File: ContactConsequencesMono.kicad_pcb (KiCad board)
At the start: 2 copper layers, 135 x 124 mm, 183 parts, among them IC1 TPD2E1B06, IC2 TPS73633, IC3 MCP73831/2-OT, IC4 TPS73618, IC5 MCP1640-SOT, IC6 TPS73633, J1 ISP, J10 PWM, J11 Sense1, J12 Sense2, J13 IO1, J14 IO2, J15 I2C, J16 Serial, J17 I2S, J2 Line in, J3 Line out, J4 SD_Card, J5 shield, J6 USB_OTG, J7 Battery, J8 Display - secondary, J9 Display - main, Q1 Q_PMOS_GSD, SW1 Reset, SW2 Charge select, SW3 sw_vol, SW4 Rotary_Encoder, SW5 sw_fadein, SW6 sw_fadeout, SW7 sw_touch, SW8 sw_mode, SW9 sw_release, U1 ATMEGA32U4-AU, U2 vs1053b, U3 MAX9723-TQFN, U4 MAX7219, U5 TCA9534, U6 TXS0108EPWR, Y1 16MHz, Y2 12,288MHz

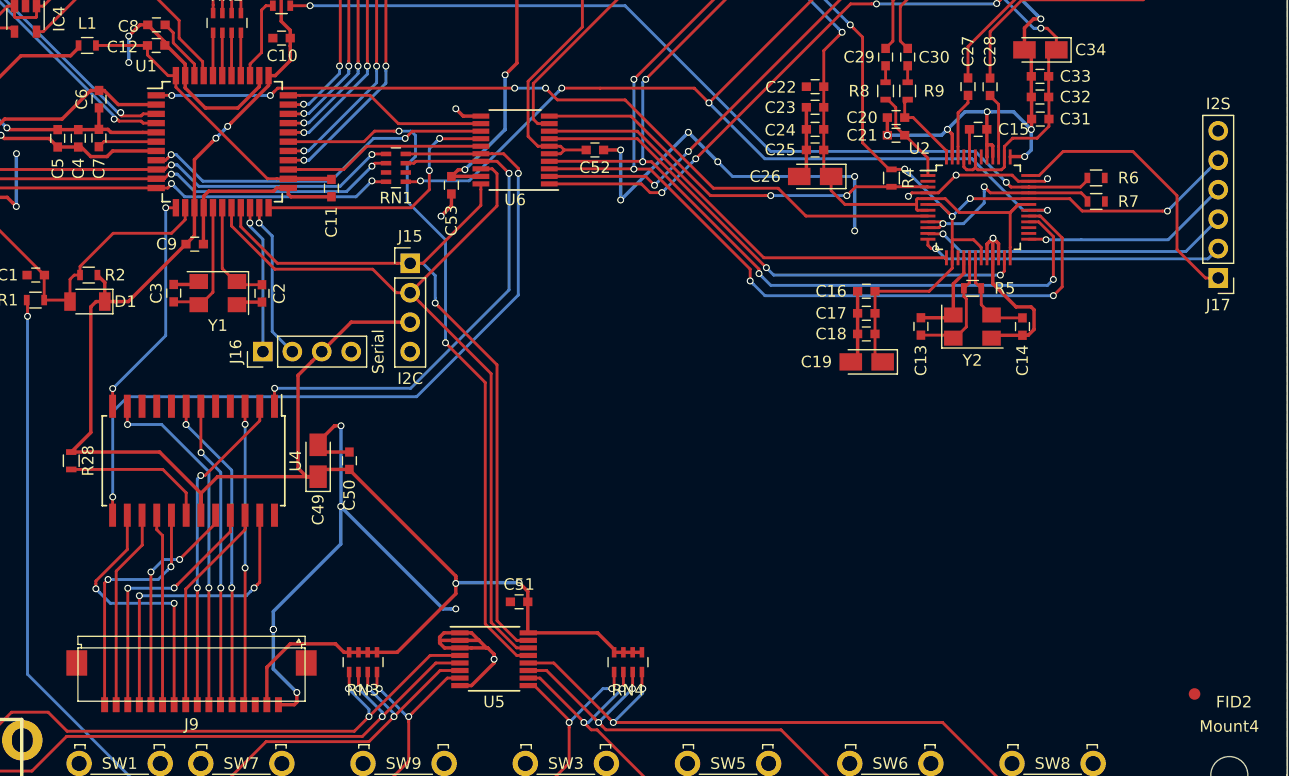
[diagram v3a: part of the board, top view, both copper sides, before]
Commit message: v0.1 ok for fab. Quote asked to PCB maker.
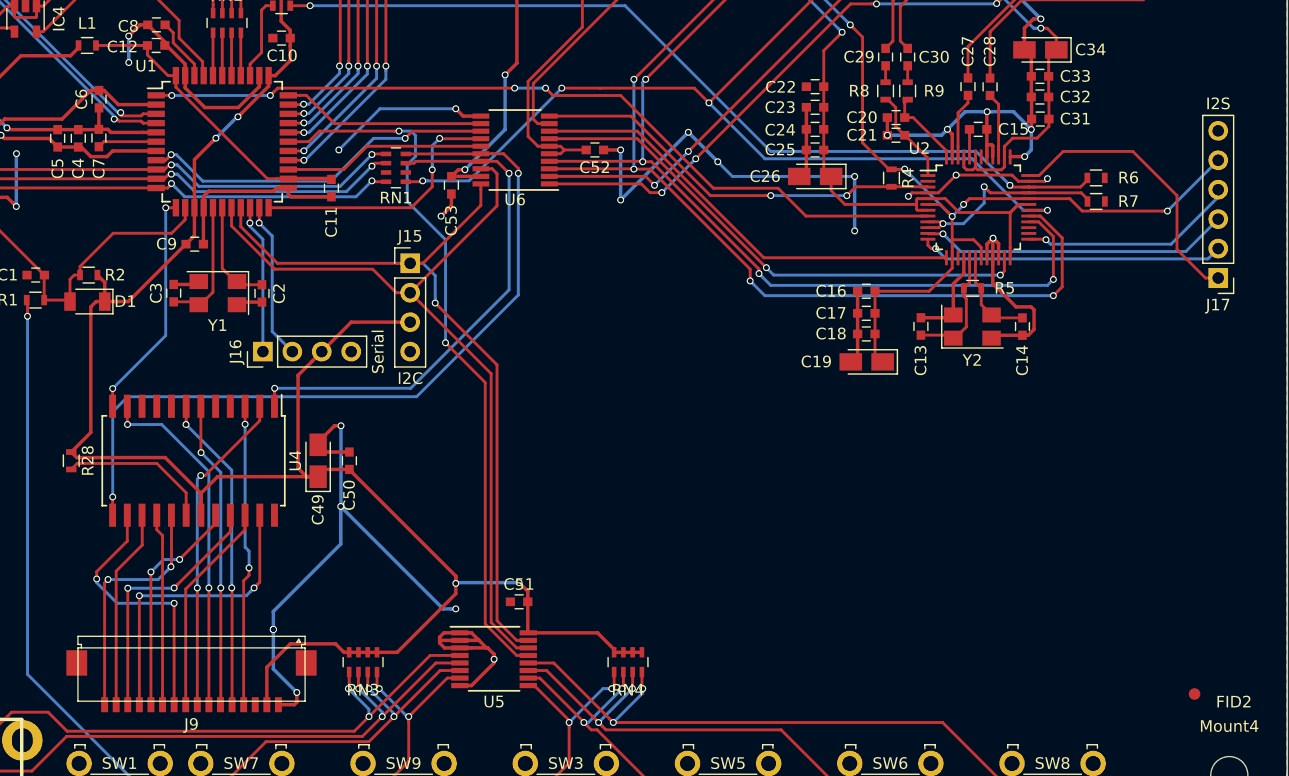
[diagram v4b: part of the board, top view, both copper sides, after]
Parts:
- added svg2mod: G***, Logos:cc_Silk_60mm, B.Cu at (171.1, 117.6)
- added svg2mod: G***, Logos:cc_noms, B.Cu at (145.2, 134.0)
- added svg2mod: G***, Logos:cc_capacitivemusicplayer, B.Cu at (148.8, 66.3)
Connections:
- SW4 pad 4: DGND -> (no net)
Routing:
- net DGND: track 342.5 -> 354.1 mm, vias 33 -> 34
- net I2S_MCK: track 18.2 -> 18.8 mm
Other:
- board text added: "XI/2017"
- board text added: "v0.1"

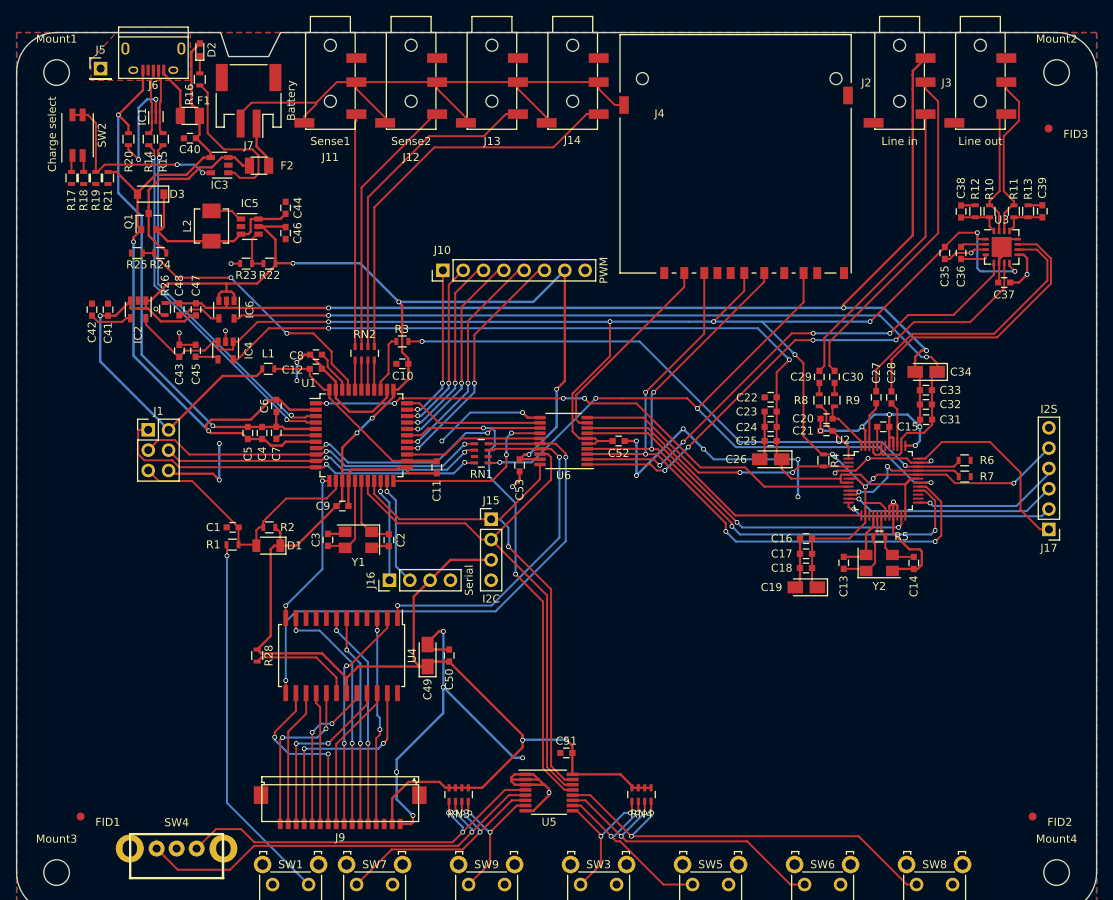
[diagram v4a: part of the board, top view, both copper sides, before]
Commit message: Updated project with connector for main power switch. Modified fabrication files.
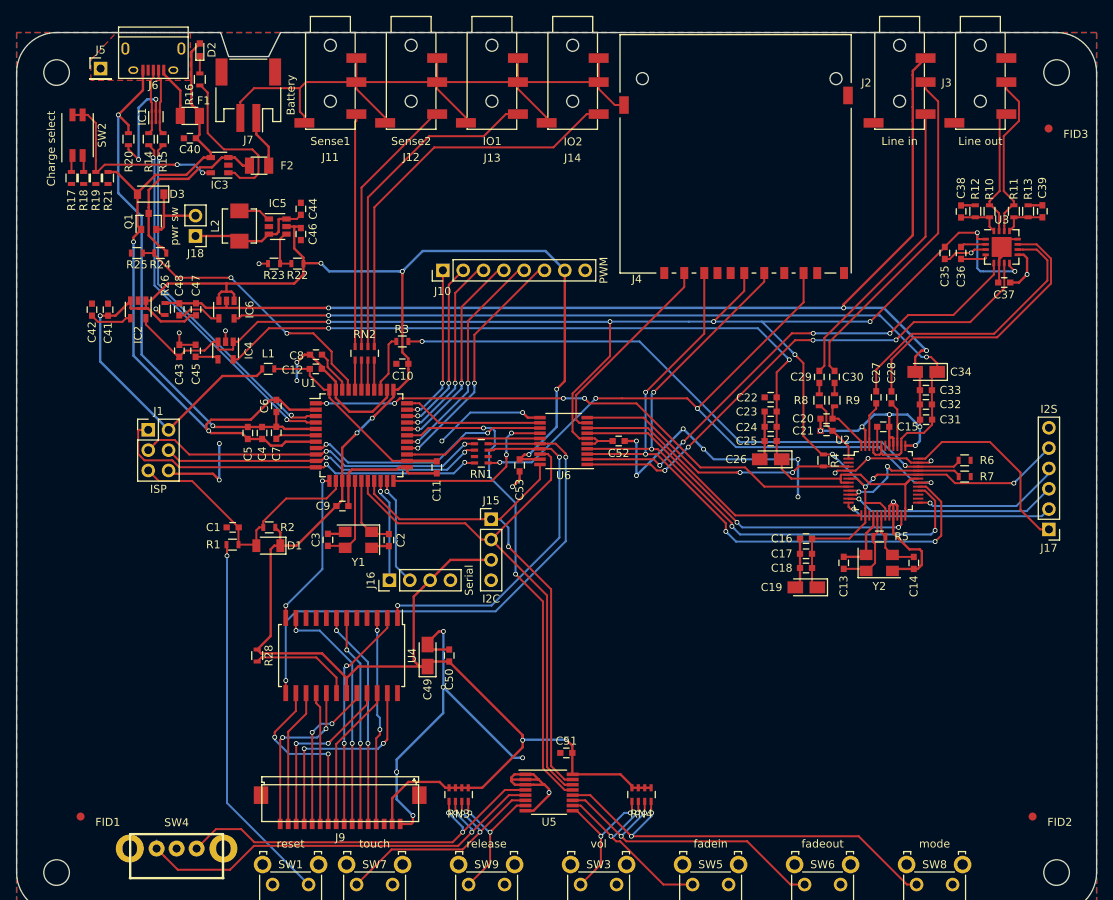
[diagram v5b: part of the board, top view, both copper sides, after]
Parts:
- added J18: pwr sw, Pin_Headers:Pin_Header_Straight_1x02_Pitch2.54mm, F.Cu at (102.4, 65.4)
- SW1: value Reset -> reset
- SW3: value sw_vol -> vol
- SW5: value sw_fadein -> fadein
- SW6: value sw_fadeout -> fadeout
- SW7: value sw_touch -> touch
- SW8: value sw_mode -> mode
- SW9: value sw_release -> release
- moved svg2mod 5.71 mm to (154.0, 63.9)
- moved R22 3.49 mm to (115.1, 68.9)
- moved IC5 3.49 mm to (112.6, 64.3)
- moved L2 3.49 mm to (107.9, 64.2)
- moved R23 3.49 mm to (112.2, 68.9)
- moved C46 1.91 mm to (115.5, 65.2)
- moved C44 1.91 mm to (115.5, 62.0)
- moved J7 0.70 mm to (109.0, 47.8)
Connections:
- D3 pad 1: Net-(C44-Pad1) -> Net-(D3-Pad1)
- J4 pad 10: (no net) -> Net-(J4-Pad10)
- J4 pad 11: (no net) -> Net-(J4-Pad11)
- J4 pad 8: (no net) -> Net-(J4-Pad8)
- J4 pad 9: (no net) -> Net-(J4-Pad9)
- J6 pad 4: (no net) -> Net-(J6-Pad4)
- J8 pad 14: (no net) -> Net-(J8-Pad14)
- J9 pad 3: (no net) -> Net-(J9-Pad3)
- Q1 pad 2: Net-(C44-Pad1) -> Net-(D3-Pad1)
- RN1 pad 2: (no net) -> Net-(RN1-Pad2)
- RN1 pad 7: (no net) -> Net-(RN1-Pad7)
- SW1 pad : DGND -> (no net)
- SW3 pad : DGND -> (no net)
- SW5 pad : DGND -> (no net)
- SW6 pad : DGND -> (no net)
- SW7 pad : DGND -> (no net)
- SW8 pad : DGND -> (no net)
- SW9 pad : DGND -> (no net)
- U2 pad 15: (no net) -> Net-(U2-Pad15)
- U2 pad 2: (no net) -> Net-(U2-Pad2)
- U2 pad 26: (no net) -> Net-(U2-Pad26)
- U2 pad 27: (no net) -> Net-(U2-Pad27)
- U2 pad 42: (no net) -> Net-(U2-Pad42)
- U4 pad 10: (no net) -> /Leds/DIG_5
- U4 pad 24: (no net) -> Net-(U4-Pad24)
- U4 pad 5: (no net) -> /Leds/DIG_6
- U4 pad 8: (no net) -> /Leds/DIG_7
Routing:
- net DGND: track 354.1 -> 369.0 mm
- net Net-(D3-Pad1): track 0.00 -> 9.14 mm
- net Net-(C44-Pad1): track 24.3 -> 16.6 mm
- net +5V: track 333.2 -> 334.2 mm
- net Net-(F2-Pad1): track 5.91 -> 6.62 mm

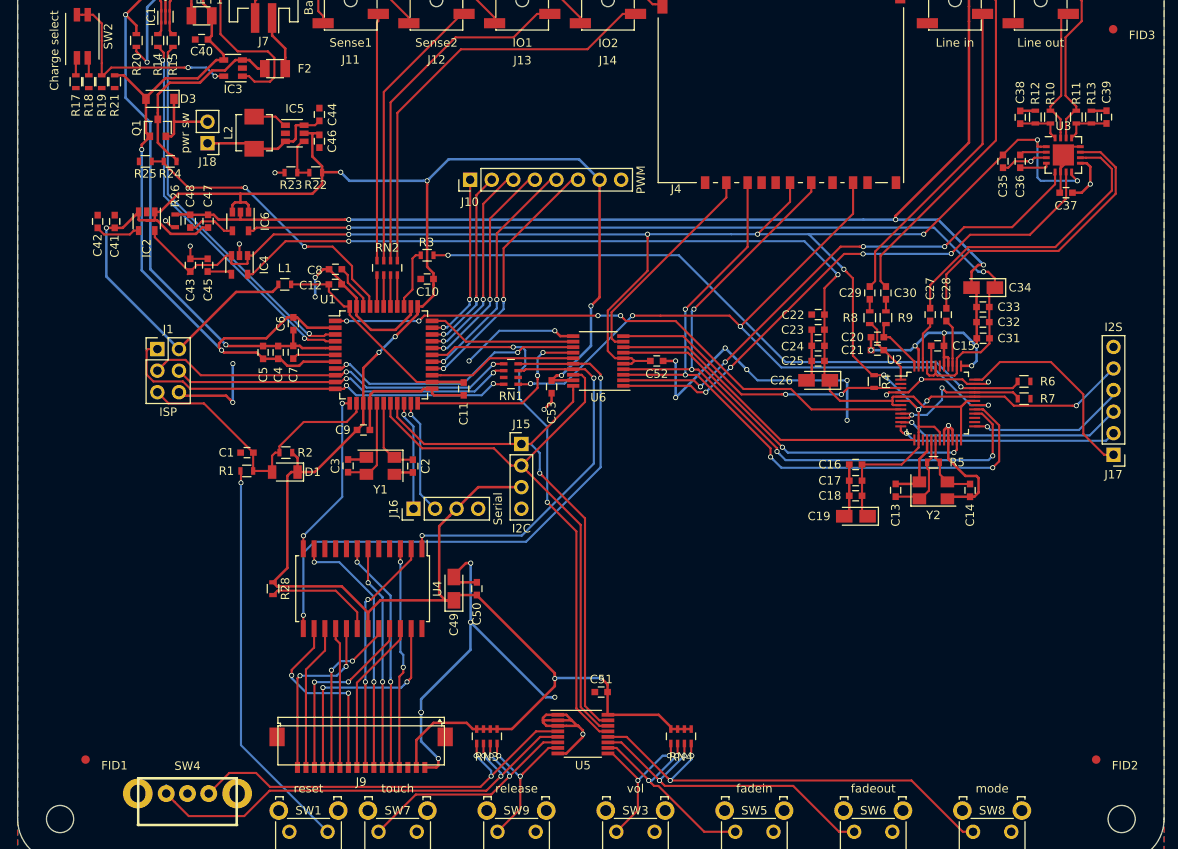
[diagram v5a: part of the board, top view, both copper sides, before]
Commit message: v0.2 ready for fabrication. Voltage regulators replaced by cheaper ones.
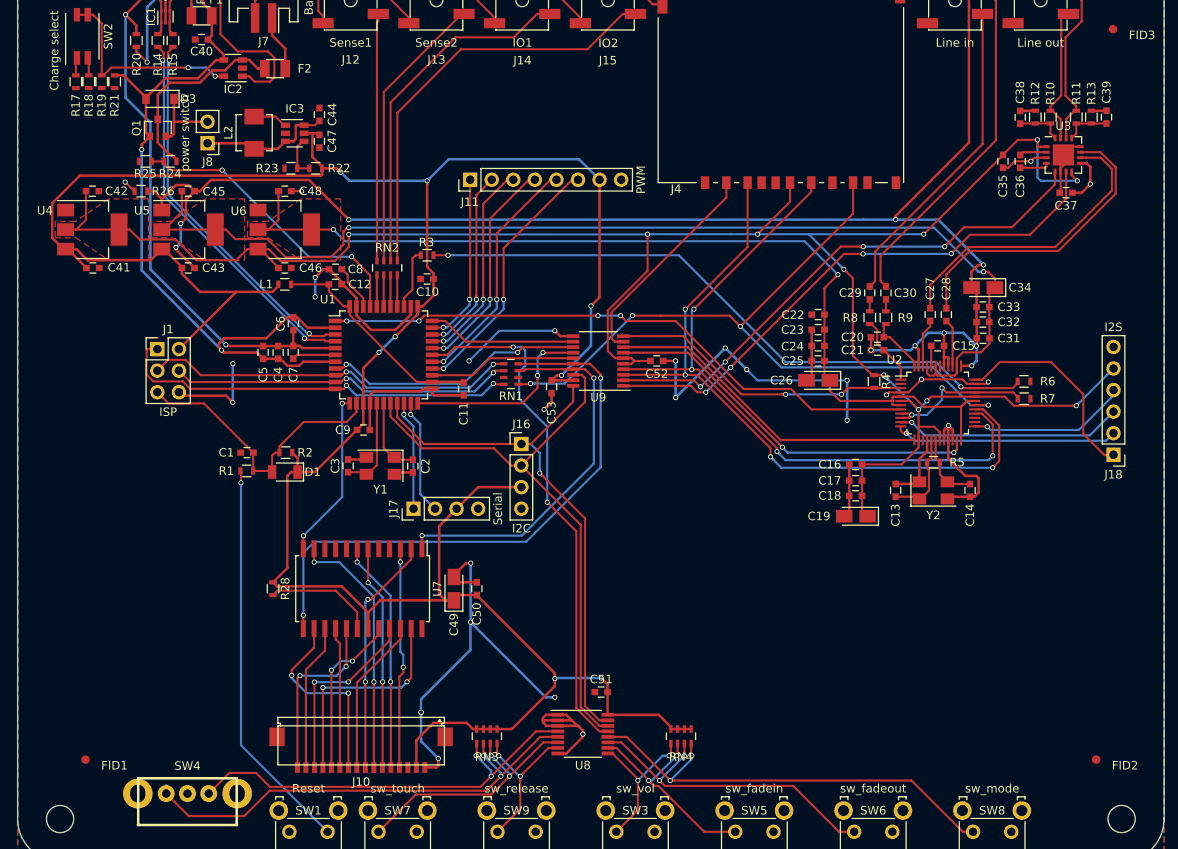
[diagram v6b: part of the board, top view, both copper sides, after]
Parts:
- removed the C47 at (102.4, 74.6)
- removed the IC2 at (95.2, 74.6)
- removed IC4: TPS73618, TO_SOT_Packages_SMD:SOT-23-5
- removed IC6: TPS73633, TO_SOT_Packages_SMD:SOT-23-5
- added C46: 100n, Capacitors_SMD:C_0603, F.Cu at (111.5, 80.1)
- added U4: LD1117S33TR_SOT223, TO_SOT_Packages_SMD:SOT-223-3_TabPin2, F.Cu at (88.8, 75.6)
- added U5: LD1117S33TR_SOT223, TO_SOT_Packages_SMD:SOT-223-3_TabPin2, F.Cu at (100.1, 75.6)
- added U6: LD1117S18TR_SOT223, TO_SOT_Packages_SMD:SOT-223-3_TabPin2, F.Cu at (111.5, 75.6)
- C42, C45, C48: value 10n -> 10u
- J8: renamed from J18; value pwr sw -> power switch
- SW1: value reset -> Reset
- SW3: value vol -> sw_vol
- SW5: value fadein -> sw_fadein
- SW6: value fadeout -> sw_fadeout
- SW7: value touch -> sw_touch
- SW8: value mode -> sw_mode
- SW9: value release -> sw_release
- moved C48 11.7 mm to (111.5, 71.1), turned to 0 degrees
- moved C45 9.01 mm to (100.1, 71.1), turned to 0 degrees
- moved C41 6.05 mm to (88.9, 80.1), turned to 0 degrees
- moved R26 5.33 mm to (94.5, 71.1), turned to 180 degrees
- moved C42 3.62 mm to (88.8, 71.1), turned to 0 degrees
- moved R22 0.51 mm to (115.1, 68.4)
- moved R23 0.51 mm to (112.2, 68.4)
- moved C43 0.42 mm to (100.1, 80.1), turned to 0 degrees
- renumbered C46 to C47, IC3 to IC2, IC5 to IC3, J9 to J10, J10 to J11, J11 to J12, J12 to J13, J13 to J14, J14 to J15, J15 to J16, J16 to J17, J17 to J18, J8 to J9, U4 to U7, U5 to U8, U6 to U9
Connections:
- C42 pad 1: Net-(C42-Pad1) -> +3V3
- C43 pad 1: +3V3 -> +5V
- C43 pad 2: DGND -> AGND
- C45 pad 1: Net-(C45-Pad1) -> +3.3VA
- C45 pad 2: DGND -> AGND
- C48 pad 1: Net-(C48-Pad1) -> +1V8
- C48 pad 2: AGND -> DGND
- J3 pad 4: DGND -> (no net)
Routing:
- net +3.3VA: track 110.7 -> 130.0 mm
- net AGND: track 172.0 -> 190.2 mm, vias 8 -> 10
- net +3V3: track 235.2 -> 252.3 mm
- net Net-(C48-Pad1): track 5.74 -> 0.00 mm
- net Net-(C42-Pad1): track 5.36 -> 0.00 mm
- net +5V: track 334.2 -> 339.3 mm, vias 10 -> 9
- net DGND: track 369.0 -> 364.2 mm, vias 34 -> 32
- net +1V8: track 112.4 -> 116.4 mm
- net Net-(C45-Pad1): track 2.93 -> 0.00 mm
- net BATT_LEVEL: track 34.5 -> 35.2 mm
- net Net-(IC3-Pad4): track 5.56 -> 5.05 mm
- added copper zone on F.Cu, net +1V8
- added copper zone on F.Cu, net +3.3VA
- added copper zone on F.Cu, net +3V3
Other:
- board text added: "v0.2"
- board text removed: "v0.1"
